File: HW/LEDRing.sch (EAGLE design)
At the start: 36 parts, among them U1 ATMEGA328P-AU, U2 MCP73831, U3 MIC5219 3.3V, U4 MMA8452Q, Y1 16MHZ

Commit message: Updated schematics.
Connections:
- new net N$31: U$1.3V3OUT, U$1.VCCIO
- net RESET: now also U$1.DTR
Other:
- note added: "Updates: -Tied VCCIO and 3V3OUT -Tied DTR to RESET"
- note removed: "Battery: https://www.sparkfun.com/products/13851"
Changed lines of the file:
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@@
 <sheet>
 <plain>
-<text x="-83.82" y="25.4" size="1.778" layer="91">Battery: https://www.sparkfun.com/products/13851</text>
+<text x="-66.04" y="25.4" size="1.778" layer="91">Updates:
+-Tied VCCIO and 3V3OUT
+-Tied DTR to RESET</text>
 </plain>
 <instances>
@@
 <label x="114.3" y="81.28" size="1.778" layer="95"/>
 </segment>
+<segment>
+<pinref part="U$1" gate="G$1" pin="DTR"/>
+<wire x1="5.08" y1="81.28" x2="7.62" y2="81.28" width="0.1524" layer="91"/>
+<label x="7.62" y="81.28" size="1.778" layer="95"/>
+</segment>
 </net>
 <net name="N$9" class="0">
@@
 </segment>
 </net>
+<net name="N$31" class="0">
+<segment>
+<pinref part="U$1" gate="G$1" pin="VCCIO"/>
+<wire x1="-25.4" y1="83.82" x2="-30.48" y2="83.82" width="0.1524" layer="91"/>
+<wire x1="-30.48" y1="83.82" x2="-30.48" y2="81.28" width="0.1524" layer="91"/>
+<pinref part="U$1" gate="G$1" pin="3V3OUT"/>
+<wire x1="-30.48" y1="81.28" x2="-25.4" y2="81.28" width="0.1524" layer="91"/>
+</segment>
+</net>
 </nets>
 </sheet>
@@
 </schematic>
 </drawing>
+<compatibility>
+<note version="6.3" minversion="6.2.2" severity="warning">
+Since Version 6.2.2 text objects can contain more than one line,
+which will not be processed correctly with this version.
+</note>
+</compatibility>
 </eagle>

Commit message: Adding PCB changes for next version.
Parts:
- added C8: (no value), SparkFun-Capacitors:CAP0603-CAP
- added D13: (no value), SparkFun-LED:LED0603
- added JP1, JP2: JUMPER-3SMD, SparkFun-Retired:JUMPER-3SMD
- added JP3: JUMPER-3-OLDSMD, SparkFun-Retired:JUMPER-3-OLDSMD
- added LOGO1: OSHW-LOGOMINI, SparkFun-Aesthetics:OSHW-LOGOMINI
- added R9: (no value), SparkFun-Passives:RESISTOR0603-RES
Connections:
- new net N$32: C8.1, U$1.DTR
- new net N$33: R9.2, U1.PB1
- new net N$34: D13.A, R9.1
- net GND: now also D13.C
- net RESET: now also C8.2; no longer U$1.DTR
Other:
- note removed: "Updates: -Tied VCCIO and 3V3OUT -Tied DTR to RESET"
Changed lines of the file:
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@@
 <part name="U$2" library="LEDRingLib" deviceset="TE_USB_A121025CT" device=""/>
 <part name="R8" library="SparkFun-Passives" deviceset="RESISTOR" device="0603-RES"/>
+<part name="C8" library="SparkFun-Capacitors" deviceset="CAP" device="0603-CAP"/>
+<part name="D13" library="SparkFun-LED" deviceset="LED" device="0603"/>
+<part name="R9" library="SparkFun-Passives" deviceset="RESISTOR" device="0603-RES"/>
+<part name="GND19" library="SparkFun-Aesthetics" deviceset="GND" device=""/>
+<part name="LOGO1" library="SparkFun-Aesthetics" deviceset="OSHW-LOGO" device="MINI"/>
+<part name="JP1" library="SparkFun-Retired" deviceset="JUMPER-3" device="SMD"/>
+<part name="JP2" library="SparkFun-Retired" deviceset="JUMPER-3" device="SMD"/>
+<part name="JP3" library="SparkFun-Retired" deviceset="JUMPER-3-OLD" device="SMD"/>
 </parts>
 <sheets>
 <sheet>
 <plain>
-<text x="-66.04" y="25.4" size="1.778" layer="91">Updates:
--Tied VCCIO and 3V3OUT
--Tied DTR to RESET</text>
 </plain>
 <instances>
@@
 <instance part="U$2" gate="G$1" x="-88.9" y="88.9"/>
 <instance part="R8" gate="G$1" x="-106.68" y="-17.78" rot="R90"/>
+<instance part="C8" gate="G$1" x="15.24" y="81.28" rot="R90"/>
+<instance part="D13" gate="G$1" x="38.1" y="50.8"/>
+<instance part="R9" gate="G$1" x="38.1" y="60.96" rot="R90"/>
+<instance part="GND19" gate="1" x="38.1" y="40.64"/>
+<instance part="LOGO1" gate="G$1" x="-104.14" y="15.24"/>
+<instance part="JP1" gate="G$1" x="-76.2" y="33.02"/>
+<instance part="JP2" gate="G$1" x="-45.72" y="33.02"/>
+<instance part="JP3" gate="G$1" x="-5.08" y="27.94"/>
 </instances>
 <busses>
@@
 <label x="78.74" y="-88.9" size="1.778" layer="95" rot="R180"/>
 </segment>
+<segment>
+<pinref part="D13" gate="G$1" pin="C"/>
+<pinref part="GND19" gate="1" pin="GND"/>
+<wire x1="38.1" y1="45.72" x2="38.1" y2="43.18" width="0.1524" layer="91"/>
+</segment>
 </net>
 <net name="N$7" class="0">
@@
 </segment>
 <segment>
-<pinref part="U$1" gate="G$1" pin="DTR"/>
-<wire x1="5.08" y1="81.28" x2="7.62" y2="81.28" width="0.1524" layer="91"/>
-<label x="7.62" y="81.28" size="1.778" layer="95"/>
+<pinref part="C8" gate="G$1" pin="2"/>
+<wire x1="17.78" y1="81.28" x2="22.86" y2="81.28" width="0.1524" layer="91"/>
+<label x="22.86" y="81.28" size="1.778" layer="95"/>
 </segment>
 </net>
@@
 </segment>
 </net>
+<net name="N$32" class="0">
+<segment>
+<pinref part="U$1" gate="G$1" pin="DTR"/>
+<pinref part="C8" gate="G$1" pin="1"/>
+<wire x1="5.08" y1="81.28" x2="10.16" y2="81.28" width="0.1524" layer="91"/>
+</segment>
+</net>
+<net name="N$33" class="0">
+<segment>
+<pinref part="U1" gate="A" pin="PB1"/>
+<wire x1="76.2" y1="71.12" x2="38.1" y2="71.12" width="0.1524" layer="91"/>
+<pinref part="R9" gate="G$1" pin="2"/>
+<wire x1="38.1" y1="71.12" x2="38.1" y2="66.04" width="0.1524" layer="91"/>
+</segment>
+</net>
+<net name="N$34" class="0">
+<segment>
+<pinref part="R9" gate="G$1" pin="1"/>
+<pinref part="D13" gate="G$1" pin="A"/>
+<wire x1="38.1" y1="55.88" x2="38.1" y2="53.34" width="0.1524" layer="91"/>
+</segment>
+</net>
 </nets>
 </sheet>
@@
 </schematic>
 </drawing>
-<compatibility>
-<note version="6.3" minversion="6.2.2" severity="warning">
-Since Version 6.2.2 text objects can contain more than one line,
-which will not be processed correctly with this version.
-</note>
-</compatibility>
 </eagle>

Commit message: Updated to version 1.1.
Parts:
- removed JP3: JUMPER-3-OLDSMD, SparkFun-Retired:JUMPER-3-OLDSMD
- removed U$1: FT232R, GeekAmmo:FT232R
- added JP4: JUMPER-3SMD, SparkFun-Retired:JUMPER-3SMD
- added R10: 0, SparkFun-Passives:RESISTOR0603-RES
- added U5: FT231XS, SparkFun-DigitalIC:FT231XS
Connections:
- removed net N$31: U$1.3V3OUT, U$1.VCCIO
- removed net N$32: C8.1, U$1.DTR
- new net DTR: JP4.3, U5.!DTR
- new net D_N_IN: JP1.1, JP2.1, U5.USBDM
- new net D_N_OUT: JP1.2, U$2.D-
- new net D_P_IN: JP1.3, JP2.3, U5.USBDP
- new net D_P_OUT: JP2.2, U$2.D+
- new net RTS: JP4.1, U5.!RTS
- new net RTS_OR_DTR: C8.1, JP4.2
- net 5V: now also R10.2, U5.VCC; no longer U$1.VCC, U$2.VBUS
- net GND: now also U5.GND@16, U5.GND@6; no longer U$1.AGND, U$1.GND@18, U$1.GND@21, U$1.GND@7, U$1.TEST
- net N$4: now also R10.1, U$2.VBUS; no longer U$1.USBDM, U$2.D-
- net N$5: now also U5.!RESET, U5.3V3OUT, U5.VCCIO; no longer U$1.USBDP, U$2.D+
- net RX: now also U5.TXD; no longer U$1.TXD
- net TX: now also U5.RXD; no longer U$1.RXD
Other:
- note added: "Battery: 1.185 x 1.42"
- moved on the sheet: C2, C4, C8, JP1, JP2

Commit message: Found error for USB part. Fixed. Still need to move usb to original spot.
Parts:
- removed U$2: TE_USB_A121025CT, LEDRingLib:TE_USB_A121025CT
- added R11, R12: 10k, SparkFun-Passives:RESISTOR0603-RES
- added U$1: TE_USB_A121025CT, LEDRingLib:TE_USB_A121025CT
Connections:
- new net INT1: R11.1, U1.PD2, U4.INT1
- new net INT2: R12.1, U1.PD3, U4.INT2
- net D_N_OUT: now also U$1.D-; no longer U$2.D-
- net D_P_OUT: now also U$1.D+; no longer U$2.D+
- net GND: now also U$1.GND; no longer U$2.GND
- net N$4: now also U$1.VBUS; no longer U$2.VBUS
- net RX: no longer U4.INT2
- net TX: no longer U4.INT1
- net V3_3: now also R11.2, R12.2
- net VSTAT: now also U1.PD4; no longer U1.PD3
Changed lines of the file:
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@@
 <part name="D12" library="SparkFun-LED" deviceset="WS2812B" device=""/>
 <part name="J3" library="SparkFun-Connectors" deviceset="M02" device="PTH"/>
-<part name="U$2" library="LEDRingLib" deviceset="TE_USB_A121025CT" device=""/>
 <part name="R8" library="SparkFun-Passives" deviceset="RESISTOR" device="0603-RES"/>
 <part name="C8" library="SparkFun-Capacitors" deviceset="CAP" device="0603-CAP"/>
@@
 <part name="GND20" library="SparkFun-Aesthetics" deviceset="GND" device=""/>
 <part name="JP4" library="SparkFun-Retired" deviceset="JUMPER-3" device="SMD"/>
+<part name="U$1" library="LEDRingLib" deviceset="TE_USB_A121025CT" device=""/>
+<part name="R11" library="SparkFun-Passives" deviceset="RESISTOR" device="0603-RES" value="10k"/>
+<part name="R12" library="SparkFun-Passives" deviceset="RESISTOR" device="0603-RES" value="10k"/>
 </parts>
 <sheets>
@@
 <instance part="D12" gate="G$1" x="99.06" y="-83.82" rot="MR0"/>
 <instance part="J3" gate="G$1" x="-2.54" y="-10.16" rot="R180"/>
-<instance part="U$2" gate="G$1" x="-96.52" y="104.14"/>
 <instance part="R8" gate="G$1" x="-106.68" y="-17.78" rot="R90"/>
 <instance part="C8" gate="G$1" x="-10.16" y="22.86"/>
@@
 <instance part="GND20" gate="1" x="-27.94" y="63.5"/>
 <instance part="JP4" gate="G$1" x="-12.7" y="35.56"/>
+<instance part="U$1" gate="G$1" x="-99.06" y="104.14"/>
+<instance part="R11" gate="G$1" x="132.08" y="20.32" rot="R90"/>
+<instance part="R12" gate="G$1" x="142.24" y="20.32" rot="R90"/>
 </instances>
 <busses>
@@
 </segment>
 <segment>
-<pinref part="U4" gate="G$1" pin="INT2"/>
-<wire x1="104.14" y1="12.7" x2="106.68" y2="12.7" width="0.1524" layer="91"/>
-<label x="106.68" y="12.7" size="1.778" layer="95"/>
-</segment>
-<segment>
 <pinref part="U5" gate="U$1" pin="TXD"/>
 <wire x1="0" y1="109.22" x2="2.54" y2="109.22" width="0.1524" layer="91"/>
@@
 <wire x1="142.24" y1="73.66" x2="144.78" y2="73.66" width="0.1524" layer="91"/>
 <label x="144.78" y="73.66" size="1.778" layer="95"/>
-</segment>
-<segment>
-<pinref part="U4" gate="G$1" pin="INT1"/>
-<wire x1="104.14" y1="10.16" x2="106.68" y2="10.16" width="0.1524" layer="91"/>
-<label x="106.68" y="10.16" size="1.778" layer="95"/>
 </segment>
 <segment>
@@
 <pinref part="GND1" gate="1" pin="GND"/>
 <wire x1="-81.28" y1="99.06" x2="-81.28" y2="83.82" width="0.1524" layer="91"/>
-<pinref part="U$2" gate="G$1" pin="GND"/>
-<wire x1="-86.36" y1="99.06" x2="-81.28" y2="99.06" width="0.1524" layer="91"/>
+<wire x1="-88.9" y1="99.06" x2="-81.28" y2="99.06" width="0.1524" layer="91"/>
+<pinref part="U$1" gate="G$1" pin="GND"/>
 </segment>
 <segment>
@@
 <label x="109.22" y="-17.78" size="1.778" layer="95"/>
 </segment>
+<segment>
+<pinref part="R11" gate="G$1" pin="2"/>
+<wire x1="132.08" y1="25.4" x2="132.08" y2="30.48" width="0.1524" layer="91"/>
+<pinref part="R12" gate="G$1" pin="2"/>
+<wire x1="132.08" y1="30.48" x2="142.24" y2="30.48" width="0.1524" layer="91"/>
+<wire x1="142.24" y1="30.48" x2="142.24" y2="25.4" width="0.1524" layer="91"/>
+<label x="134.62" y="30.48" size="1.778" layer="95"/>
+</segment>
 </net>
 <net name="SCL" class="0">
@@
 </segment>
 <segment>
-<pinref part="U1" gate="A" pin="PD3"/>
-<wire x1="111.76" y1="68.58" x2="114.3" y2="68.58" width="0.1524" layer="91"/>
-<label x="114.3" y="68.58" size="1.778" layer="95"/>
-</segment>
-<segment>
 <pinref part="R8" gate="G$1" pin="1"/>
 <wire x1="-106.68" y1="-22.86" x2="-106.68" y2="-25.4" width="0.1524" layer="91"/>
 <label x="-109.22" y="-27.94" size="1.778" layer="95"/>
+</segment>
+<segment>
+<pinref part="U1" gate="A" pin="PD4"/>
+<wire x1="111.76" y1="66.04" x2="114.3" y2="66.04" width="0.1524" layer="91"/>
+<label x="114.3" y="66.04" size="1.778" layer="95"/>
 </segment>
 </net>
@@
 <net name="D_N_OUT" class="0">
 <segment>
-<pinref part="U$2" gate="G$1" pin="D-"/>
-<wire x1="-86.36" y1="106.68" x2="-83.82" y2="106.68" width="0.1524" layer="91"/>
-<label x="-83.82" y="106.68" size="1.778" layer="95"/>
+<label x="-86.36" y="106.68" size="1.778" layer="95"/>
+<pinref part="U$1" gate="G$1" pin="D-"/>
+<wire x1="-86.36" y1="106.68" x2="-88.9" y2="106.68" width="0.1524" layer="91"/>
 </segment>
 <segment>
@@
 <net name="D_P_OUT" class="0">
 <segment>
-<pinref part="U$2" gate="G$1" pin="D+"/>
-<wire x1="-86.36" y1="104.14" x2="-83.82" y2="104.14" width="0.1524" layer="91"/>
-<label x="-83.82" y="104.14" size="1.778" layer="95"/>
+<label x="-86.36" y="104.14" size="1.778" layer="95"/>
+<pinref part="U$1" gate="G$1" pin="D+"/>
+<wire x1="-86.36" y1="104.14" x2="-88.9" y2="104.14" width="0.1524" layer="91"/>
 </segment>
 <segment>
@@
 <net name="N$4" class="0">
 <segment>
-<pinref part="U$2" gate="G$1" pin="VBUS"/>
 <pinref part="R10" gate="G$1" pin="1"/>
-<wire x1="-86.36" y1="109.22" x2="-83.82" y2="109.22" width="0.1524" layer="91"/>
-</segment>
-</net>
+<pinref part="U$1" gate="G$1" pin="VBUS"/>
+<wire x1="-83.82" y1="109.22" x2="-88.9" y2="109.22" width="0.1524" layer="91"/>
+</segment>
+</net>
+<net name="INT2" class="0">
+<segment>
+<pinref part="U4" gate="G$1" pin="INT2"/>
+<wire x1="104.14" y1="12.7" x2="106.68" y2="12.7" width="0.1524" layer="91"/>
+<label x="106.68" y="12.7" size="1.778" layer="95"/>
+</segment>
+<segment>
+<pinref part="R12" gate="G$1" pin="1"/>
+<wire x1="142.24" y1="15.24" x2="142.24" y2="12.7" width="0.1524" layer="91"/>
+<label x="139.7" y="10.16" size="1.778" layer="95"/>
+</segment>
+<segment>
+<pinref part="U1" gate="A" pin="PD3"/>
+<wire x1="111.76" y1="68.58" x2="114.3" y2="68.58" width="0.1524" layer="91"/>
+<label x="114.3" y="68.58" size="1.778" layer="95"/>
+</segment>
+</net>
+<net name="INT1" class="0">
+<segment>
+<pinref part="U4" gate="G$1" pin="INT1"/>
+<wire x1="104.14" y1="10.16" x2="106.68" y2="10.16" width="0.1524" layer="91"/>
+<label x="106.68" y="10.16" size="1.778" layer="95"/>
+</segment>
+<segment>
+<pinref part="R11" gate="G$1" pin="1"/>
+<wire x1="132.08" y1="15.24" x2="132.08" y2="12.7" width="0.1524" layer="91"/>
+<label x="129.54" y="10.16" size="1.778" layer="95"/>
+</segment>
+<segment>
+<pinref part="U1" gate="A" pin="PD2"/>
+<wire x1="111.76" y1="71.12" x2="114.3" y2="71.12" width="0.1524" layer="91"/>
+<label x="114.3" y="71.12" size="1.778" layer="95"/>
+</segment>
+</net>

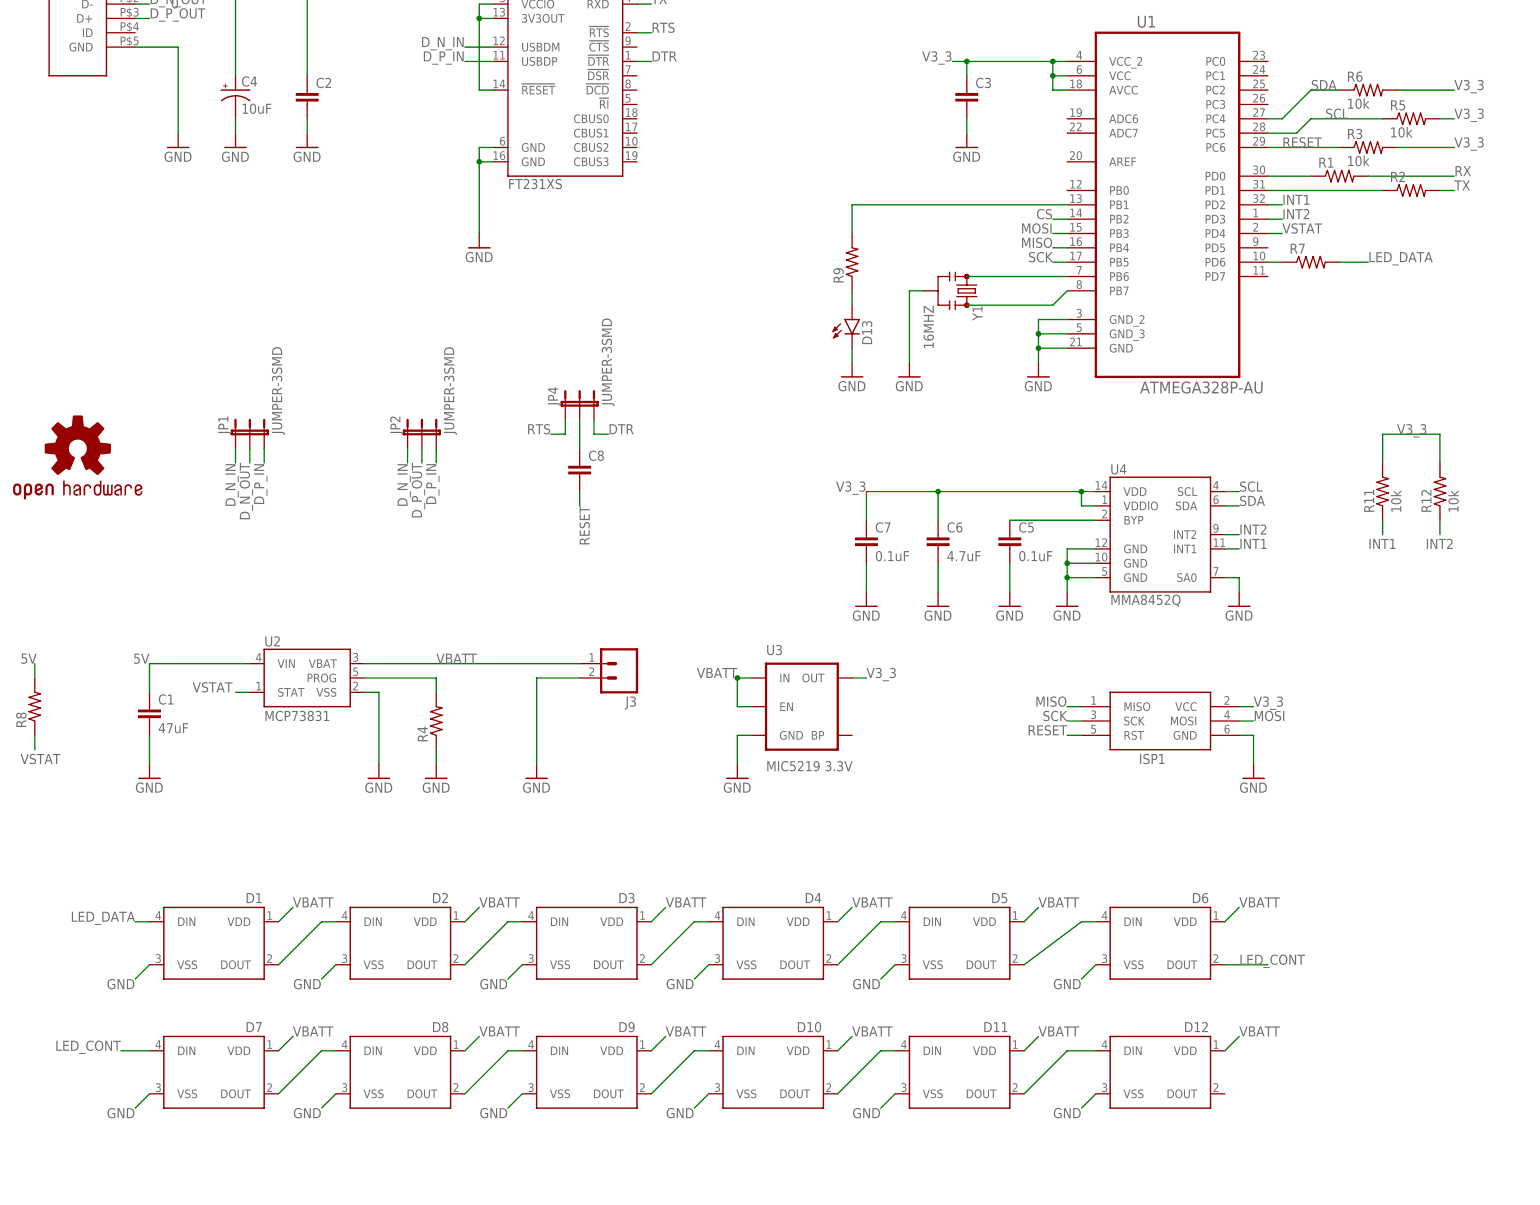
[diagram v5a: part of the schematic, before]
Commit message: Added 0.1uF and 1000uF capacitors. (Need to finish) Added values for components.
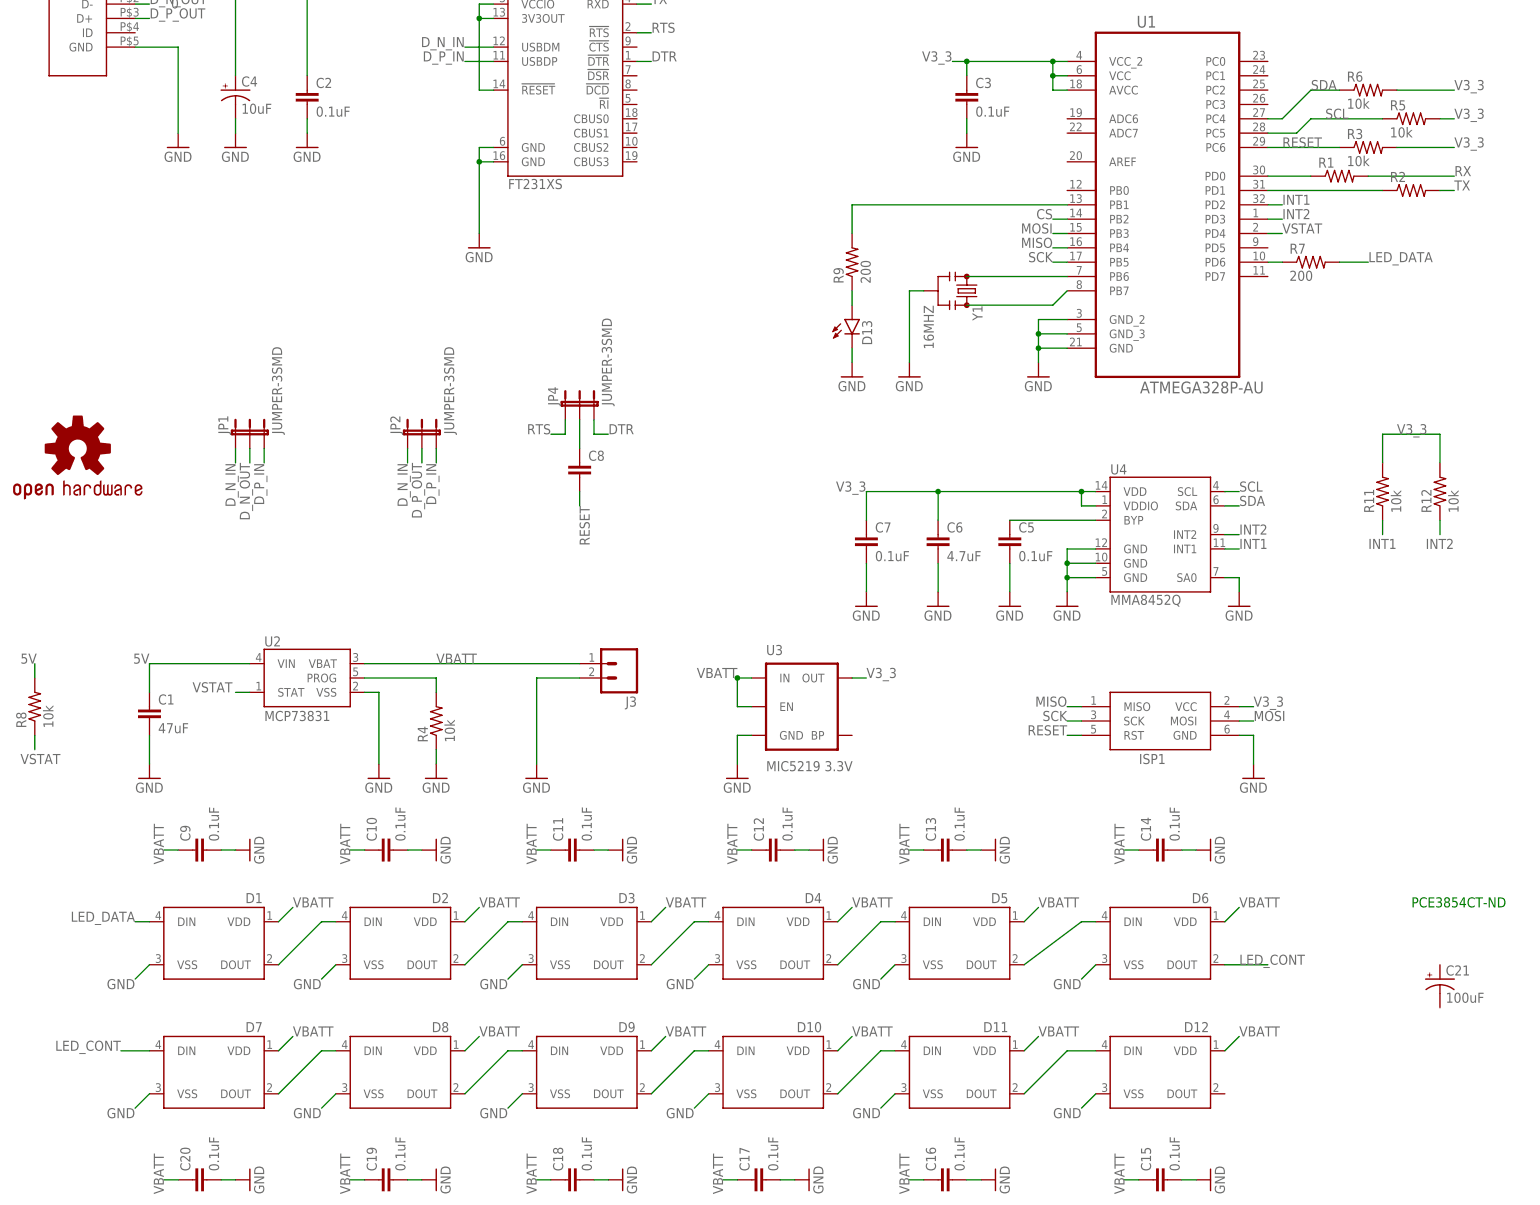
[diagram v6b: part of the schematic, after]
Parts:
- added C10, C11, C12, C13, C14, C15, C16, C17, C18, C19, C20, C9: 0.1uF, SparkFun-Capacitors:CAP0603-CAP
- added C21: 100uF, SparkFun-Capacitors:100UF-63V-20%(ELECT)
- C2, C3: value (none) -> 0.1uF
- R4, R8: value (none) -> 10k
- R7, R9: value (none) -> 200
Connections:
- net GND: now also C10.2, C11.2, C12.2, C13.2, C14.2, C15.2, C16.2, C17.2, C18.2, C19.2, C20.2, C9.2
- net VBATT: now also C10.1, C11.1, C12.1, C13.1, C14.1, C15.1, C16.1, C17.1, C18.1, C19.1, C20.1, C9.1
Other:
- note added: "PCE3854CT-ND"

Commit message: Ready for next version? Should probably double check.
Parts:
- removed C10, C11, C12, C13, C14, C15, C16, C17, C18, C19, C20, C9: 0.1uF, SparkFun-Capacitors:CAP0603-CAP
- removed C21: 100uF, SparkFun-Capacitors:100UF-63V-20%(ELECT)
- added R13: 10k, SparkFun-Passives:RESISTOR0603-RES
- added TP1: TEST-POINT3, SparkFun-Passives:TEST-POINT3
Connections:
- new net N$35: TP1.1, U$1.ID
- net GND: no longer C10.2, C11.2, C12.2, C13.2, C14.2, C15.2, C16.2, C17.2, C18.2, C19.2, C20.2, C9.2
- net INT1: now also R13.1
- net RX: now also R13.2
- net VBATT: no longer C10.1, C11.1, C12.1, C13.1, C14.1, C15.1, C16.1, C17.1, C18.1, C19.1, C20.1, C9.1
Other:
- note removed: "PCE3854CT-ND"
